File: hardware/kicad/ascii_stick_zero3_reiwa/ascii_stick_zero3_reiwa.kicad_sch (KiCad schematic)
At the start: 20 parts, among them J1 USB_B_Micro, J2 Buttons_1, J3 AVR-ISP-6, J4 Buttons_2, J5 Buttons_3, J6 Buttons_4, J7 STICK, J8 STICK_POWER, U1 ATmega32U4-A, Y1 Crystal

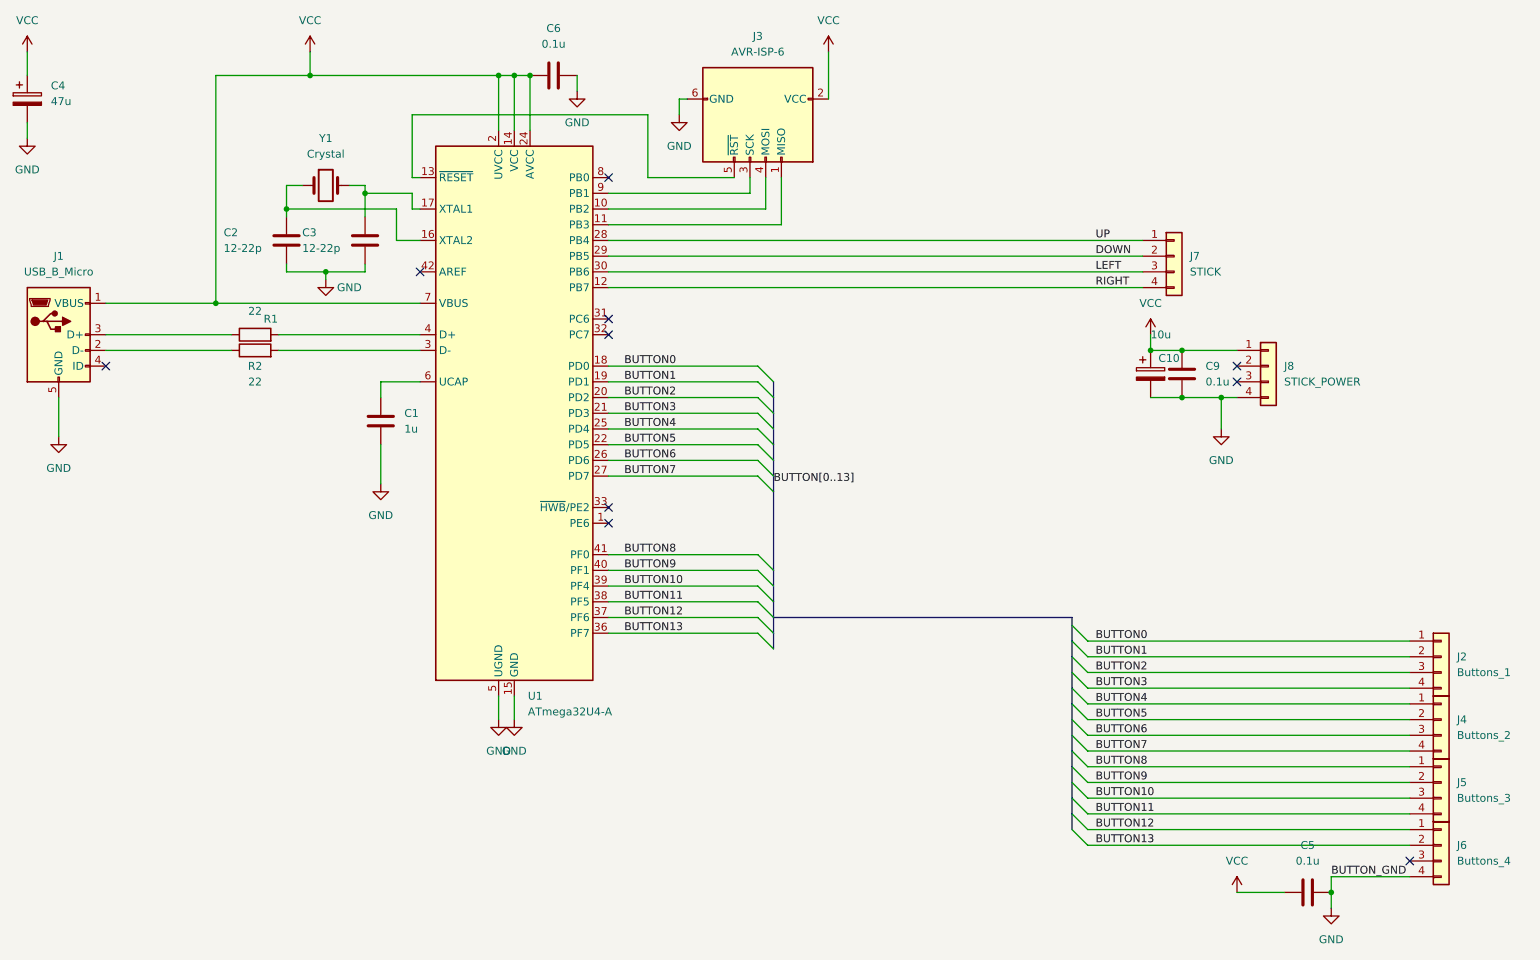
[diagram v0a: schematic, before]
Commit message: for hand-etching
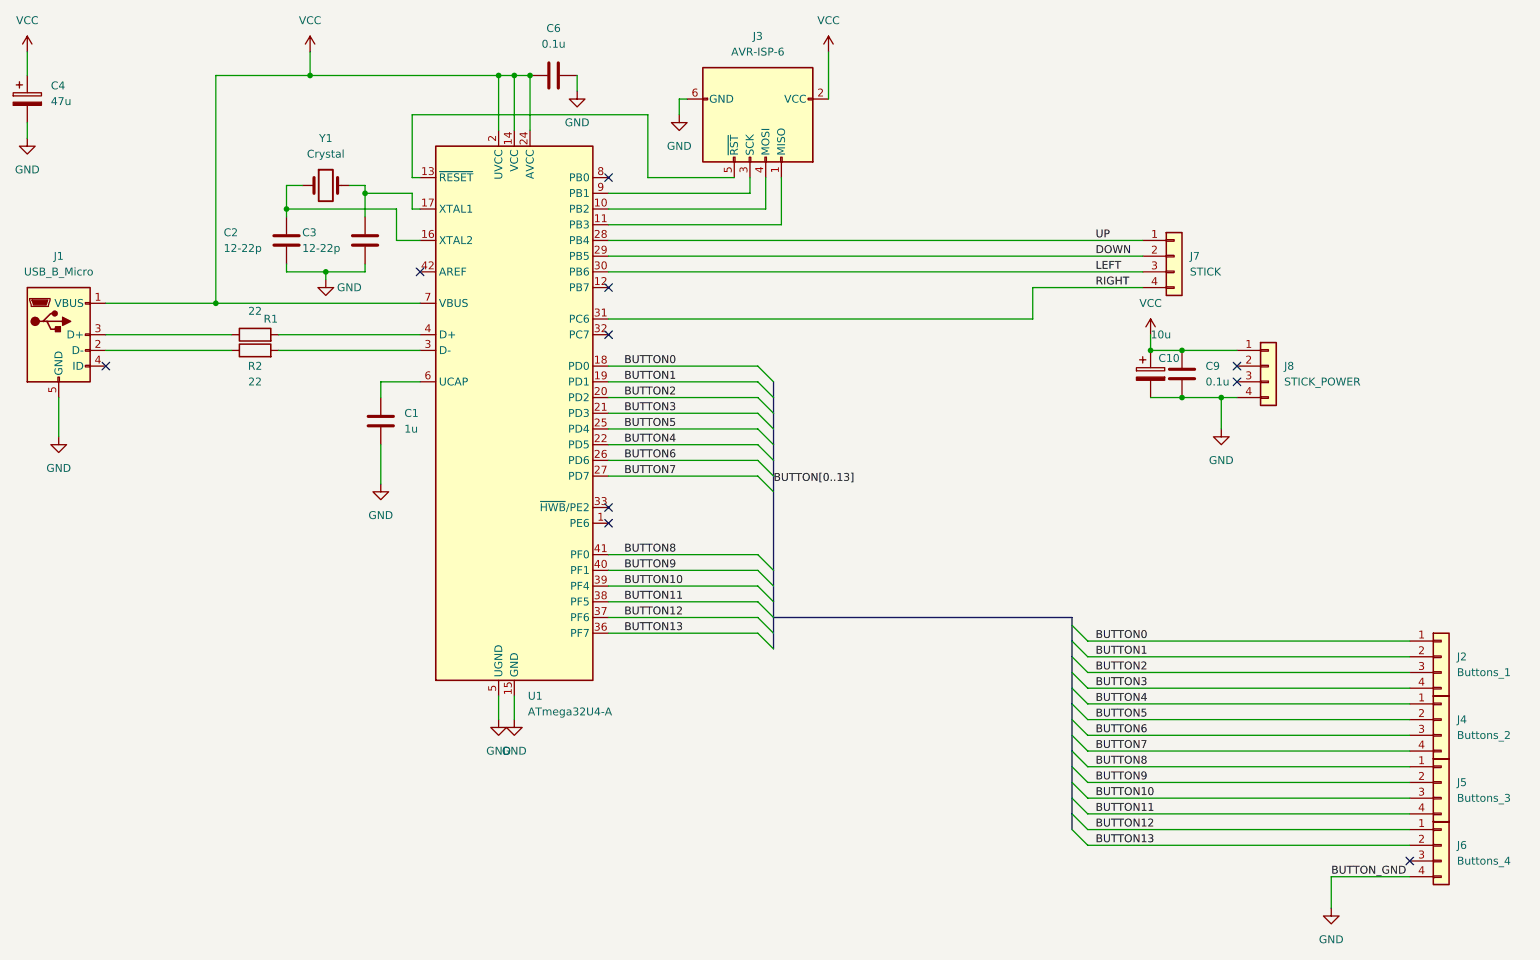
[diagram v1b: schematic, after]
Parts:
- removed C5: 0.1u, Capacitor_THT:C_Disc_D3.0mm_W2.0mm_P2.50mm, symbol Device:C
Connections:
- net BUTTON4: now also U1.22 (PD5); no longer U1.25 (PD4)
- net BUTTON5: now also U1.25 (PD4); no longer U1.22 (PD5)
- net RIGHT: now also U1.31 (PC6); no longer U1.12 (PB7)
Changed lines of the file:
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@@
   (junction (at 210.82 69.85) (diameter 0) (color 0 0 0 0)
-  )
-  (junction (at 234.95 157.48) (diameter 0) (color 0 0 0 0)
   )
   (junction (at 210.82 77.47) (diameter 0) (color 0 0 0 0)
@@
   (no_connect (at 118.11 95.25))
   (no_connect (at 36.83 72.39))
-  (no_connect (at 118.11 64.77))
+  (no_connect (at 118.11 59.69))
   (no_connect (at 118.11 41.91))
   (no_connect (at 247.65 152.4))
@@
     (stroke (width 0) (type default))
   )
+  (wire (pts (xy 186.69 59.69) (xy 204.47 59.69))
+    (stroke (width 0) (type default))
+  )
   (wire (pts (xy 66.04 57.15) (xy 72.39 57.15))
     (stroke (width 0) (type default))
@@
     (stroke (width 0) (type default))
   )
+  (wire (pts (xy 186.69 64.77) (xy 186.69 59.69))
+    (stroke (width 0) (type default))
+  )
+  (wire (pts (xy 118.11 64.77) (xy 186.69 64.77))
+    (stroke (width 0) (type default))
+  )
   (wire (pts (xy 118.11 90.17) (xy 142.24 90.17))
     (stroke (width 0) (type default))
@@
     (stroke (width 0) (type default))
   )
-  (wire (pts (xy 234.95 157.48) (xy 234.95 160.02))
+  (wire (pts (xy 234.95 154.94) (xy 234.95 160.02))
     (stroke (width 0) (type default))
   )
@@
     (stroke (width 0) (type default))
   )
-  (wire (pts (xy 234.95 154.94) (xy 234.95 157.48))
-    (stroke (width 0) (type default))
-  )
   (wire (pts (xy 195.58 124.46) (xy 247.65 124.46))
     (stroke (width 0) (type default))
@@
     (stroke (width 0) (type default))
   )
-  (wire (pts (xy 219.71 157.48) (xy 227.33 157.48))
-    (stroke (width 0) (type default))
-  )
   (wire (pts (xy 195.58 147.32) (xy 247.65 147.32))
     (stroke (width 0) (type default))
@@
     (stroke (width 0) (type default))
   )
-  (wire (pts (xy 118.11 59.69) (xy 204.47 59.69))
-    (stroke (width 0) (type default))
-  )
   (wire (pts (xy 118.11 82.55) (xy 142.24 82.55))
     (stroke (width 0) (type default))
@@
     (effects (font (size 1.27 1.27)) (justify left bottom))
   )
-  (label "BUTTON4" (at 120.65 82.55 0) (fields_autoplaced)
-    (effects (font (size 1.27 1.27)) (justify left bottom))
-  )
   (label "BUTTON0" (at 120.65 72.39 0) (fields_autoplaced)
     (effects (font (size 1.27 1.27)) (justify left bottom))
@@
     (effects (font (size 1.27 1.27)) (justify left bottom))
   )
-  (label "BUTTON5" (at 120.65 85.09 0) (fields_autoplaced)
+  (label "BUTTON5" (at 120.65 82.55 0) (fields_autoplaced)
     (effects (font (size 1.27 1.27)) (justify left bottom))
   )
@@
   )
   (label "BUTTON_GND" (at 234.95 154.94 0) (fields_autoplaced)
+    (effects (font (size 1.27 1.27)) (justify left bottom))
+  )
+  (label "BUTTON4" (at 120.65 85.09 0) (fields_autoplaced)
     (effects (font (size 1.27 1.27)) (justify left bottom))
   )
@@
         (path "/e145fb53-b9b1-46c4-af86-1b4b6edf01f5"
           (reference "R1") (unit 1)
-        )
-      )
-    )
-  )
-  (symbol (lib_id "Device:C") (at 231.14 157.48 90) (unit 1)
-    (in_bom yes) (on_board yes) (dnp no) (fields_autoplaced)
-    (property "Reference" "C5" (at 231.14 149.86 90)
-      (effects (font (size 1.27 1.27)))
-    )
-    (property "Value" "0.1u" (at 231.14 152.4 90)
-      (effects (font (size 1.27 1.27)))
-    )
-    (property "Footprint" "Capacitor_THT:C_Disc_D3.0mm_W2.0mm_P2.50mm" (at 234.95 156.5148 0)
-      (effects (font (size 1.27 1.27)) hide)
-    )
-    (property "Datasheet" "~" (at 231.14 157.48 0)
-      (effects (font (size 1.27 1.27)) hide)
-    )
-    (pin "1")
-    (pin "2")
-    (instances
-      (project "ascii_stick_zero3_reiwa"
-        (path "/e145fb53-b9b1-46c4-af86-1b4b6edf01f5"
-          (reference "C5") (unit 1)
         )
       )
@@
         )
       )
-    )
-  )
-  (symbol (lib_id "power:VCC") (at 219.71 157.48 0) (unit 1)
-    (in_bom yes) (on_board yes) (dnp no) (fields_autoplaced)
-    (property "Reference" "#PWR024" (at 219.71 161.29 0)
-      (effects (font (size 1.27 1.27)) hide)
-    )
-    (property "Value" "VCC" (at 219.71 152.4 0)
-      (effects (font (size 1.27 1.27)))
-    )
-    (property "Footprint" "" (at 219.71 157.48 0)
-      (effects (font (size 1.27 1.27)) hide)
-    )
-    (property "Datasheet" "" (at 219.71 157.48 0)
-      (effects (font (size 1.27 1.27)) hide)
-    )
-    (pin "1")
-    (instances
-      (project "ascii_stick_zero3_reiwa"
-        (path "/e145fb53-b9b1-46c4-af86-1b4b6edf01f5"
-          (reference "#PWR024") (unit 1)
-        )
-      )
